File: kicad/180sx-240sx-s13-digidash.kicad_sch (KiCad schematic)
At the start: 0 parts

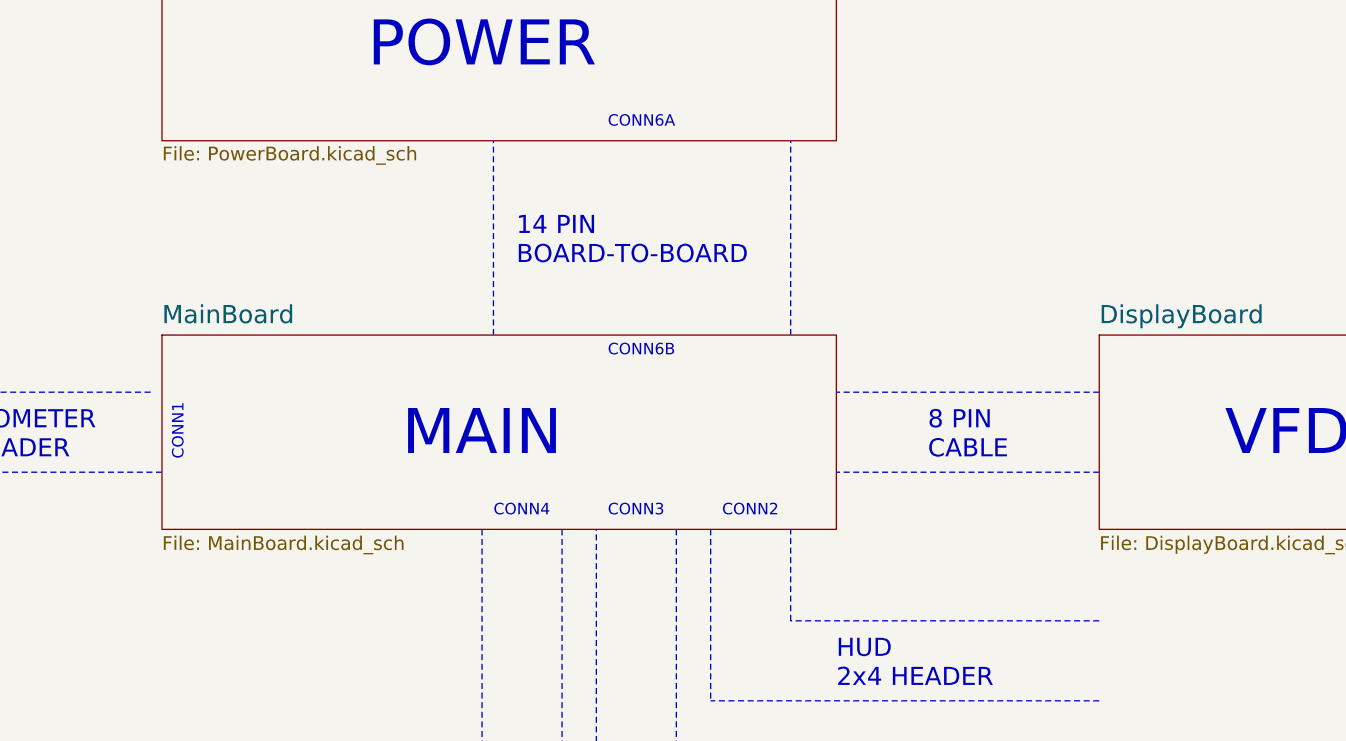
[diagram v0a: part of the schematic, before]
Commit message: Page order change and page numbers added to main block diagram.
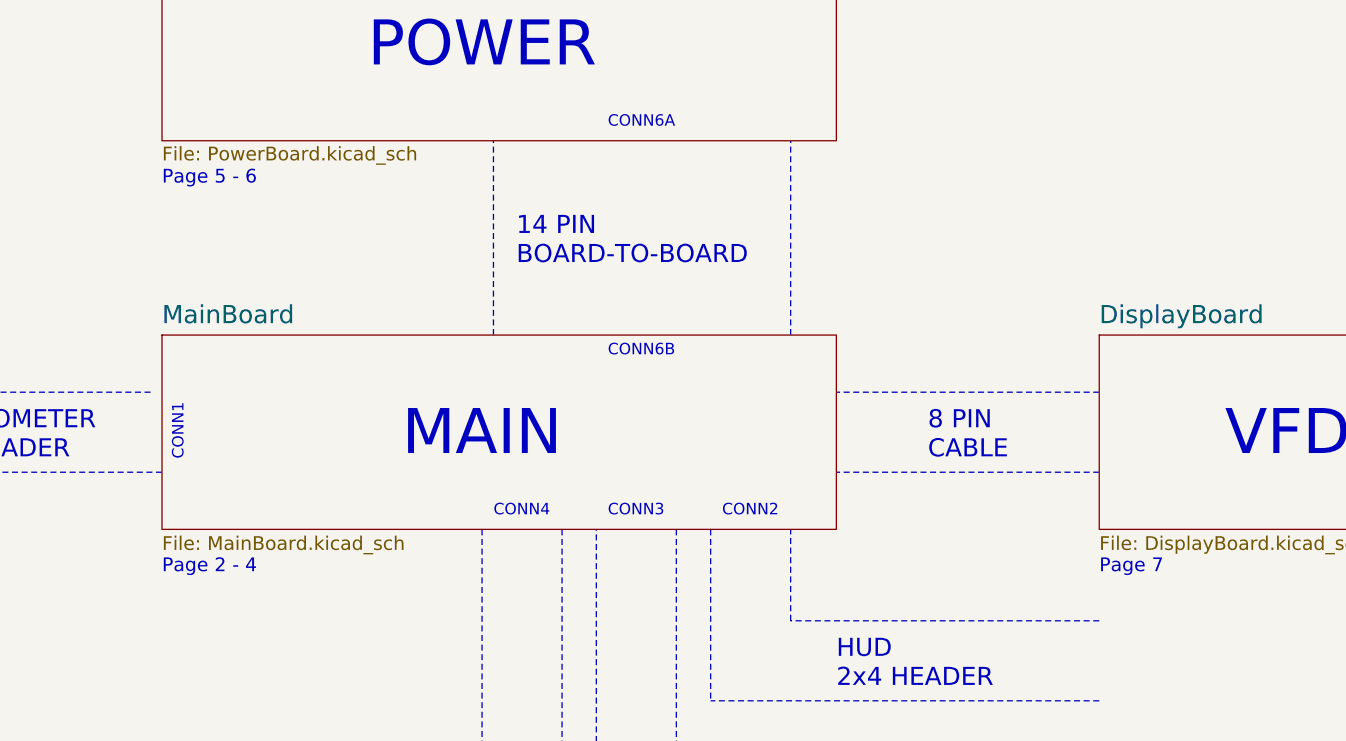
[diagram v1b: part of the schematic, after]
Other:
- note added: "Page 2 - 4"
- note added: "Page 5 - 6"
- note added: "Page 7"
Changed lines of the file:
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@@
+		)
+	)
+	(text "Page 7"
+		(exclude_from_sim no)
+		(at 203.2 104.14 0)
+		(effects
+			(font
+				(size 1.524 1.524)
+			)
+			(justify left bottom)
 		)
 	)
@@
 		)
 	)
+	(text "Page 5 - 6"
+		(exclude_from_sim no)
+		(at 99.06 60.96 0)
+		(effects
+			(font
+				(size 1.524 1.524)
+			)
+			(justify left bottom)
+		)
+	)
 	(text "POWER"
 		(exclude_from_sim no)
@@
 			(font
 				(size 1.27 1.27)
+			)
+			(justify left bottom)
+		)
+	)
+	(text "Page 2 - 4"
+		(exclude_from_sim no)
+		(at 99.06 104.14 0)
+		(effects
+			(font
+				(size 1.524 1.524)
 			)
 			(justify left bottom)
@@
 			(project "180sx-240sx-s13-digidash"
 				(path "/b719f779-5952-48c1-947f-4b13da7decde"
-					(page "4")
+					(page "2")
 				)
 			)
@@
 			(project "180sx-240sx-s13-digidash"
 				(path "/b719f779-5952-48c1-947f-4b13da7decde"
-					(page "2")
-				)
-			)
+					(page "5")
+				)
+			)
